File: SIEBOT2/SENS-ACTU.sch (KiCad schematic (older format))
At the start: 0 parts

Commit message: Added some fixes from AndroidStamp
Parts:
- added P? (x2): CONN_3X2, symbol CONN_3X2
- added P?: CONN_9X2, symbol CONN_9X2
- added P?: CONN_12X2, symbol CONN_12X2
- added P?: CONN_8X2, symbol CONN_8X2
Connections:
- new net GND: P?.2, P?.2, P?.5, P?.5
- new net I2C1_SCL_CONN: P?.4
- new net I2C1_SDA_CONN: P?.6
- new net I2C2_SCL_CONN: P?.3
- new net I2C2_SDA_CONN: P?.1
- new net STM32_ADC0: P?.1
- new net STM32_ADC1: P?.3
- new net STM32_ADC10: P?.12
- new net STM32_ADC11: P?.10
- new net STM32_ADC12: P?.8
- new net STM32_ADC13: P?.6
- new net STM32_ADC14: P?.4
- new net STM32_ADC15: P?.2
- new net STM32_ADC2: P?.5
- new net STM32_ADC3: P?.7
- new net STM32_ADC4: P?.9
- new net STM32_ADC5: P?.11
- new net STM32_ADC6: P?.13
- new net STM32_ADC7: P?.15
- new net STM32_ADC8: P?.16
- new net STM32_ADC9: P?.14
- new net STM32_PD10: P?.7
- new net STM32_PD11: P?.9
- new net STM32_PD3: P?.1
- new net STM32_PD4: P?.3
- new net STM32_PD7: P?.5
- new net STM32_PE1: P?.18
- new net STM32_PE10: P?.11
- new net STM32_PE12: P?.13
- new net STM32_PE14: P?.15
- new net STM32_PE15: P?.17
- new net STM32_PE2: P?.16
- new net STM32_PE3: P?.14
- new net STM32_PE4: P?.12
- new net STM32_PE5: P?.10
- new net STM32_PE6: P?.8
- new net STM32_PE7: P?.6
- new net STM32_PE8: P?.4
- new net STM32_PE9: P?.2
- new net TIM16_BKIN: P?.9 (P9)
- new net TIM16_CH1: P?.7 (P7)
- new net TIM17_CH1: P?.5 (P5)
- new net TIM1_BKIN: P?.2 (P2)
- new net TIM1_CH1: P?.14 (P14)
- new net TIM1_CH1N: P?.16 (P16)
- new net TIM1_CH2: P?.10 (P10)
- new net TIM1_CH2N: P?.12 (P12)
- new net TIM1_CH3: P?.6 (P6)
- new net TIM1_CH3N: P?.8 (P8)
- new net TIM1_CH4: P?.4 (P4)
- new net TIM1_ETR: P?.18 (P18)
- new net TIM2_CH1_ETR: P?.3 (P3)
- new net TIM2_CH2: P?.1 (P1)
- new net TIM3_CH1: P?.19 (P19)
- new net TIM3_CH2: P?.17 (P17)
- new net TIM3_CH3: P?.15 (P15)
- new net TIM3_CH4: P?.13 (P13)
- new net TIM3_ETR: P?.11 (P11)
- new net TIM4_CH1: P?.23 (P23)
- new net TIM4_CH2: P?.24 (P24)
- new net TIM4_CH3: P?.22 (P22)
- new net TIM4_CH4: P?.20 (P20)
- new net TIM4_ETR: P?.21 (P21)
- new net USART2_RX: P?.1, P?.6
- new net USART2_TX: P?.3, P?.4

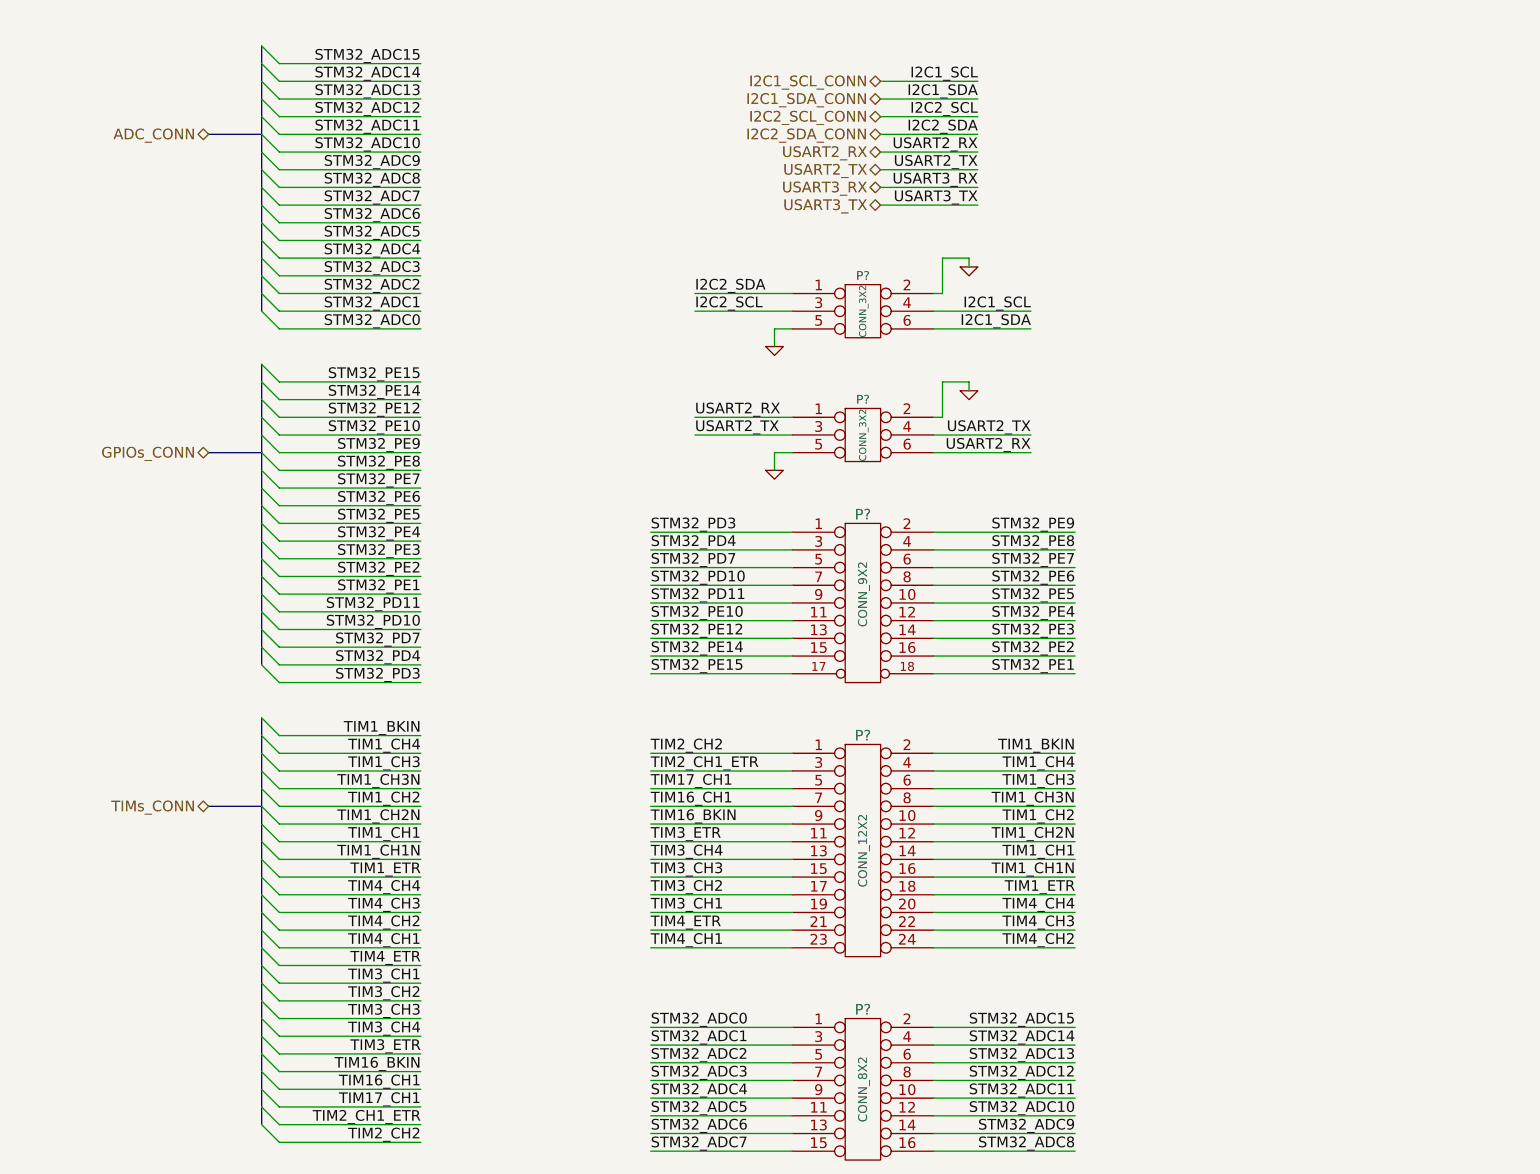
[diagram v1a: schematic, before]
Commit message: Added power dc-dc, fixed stm32 control pins
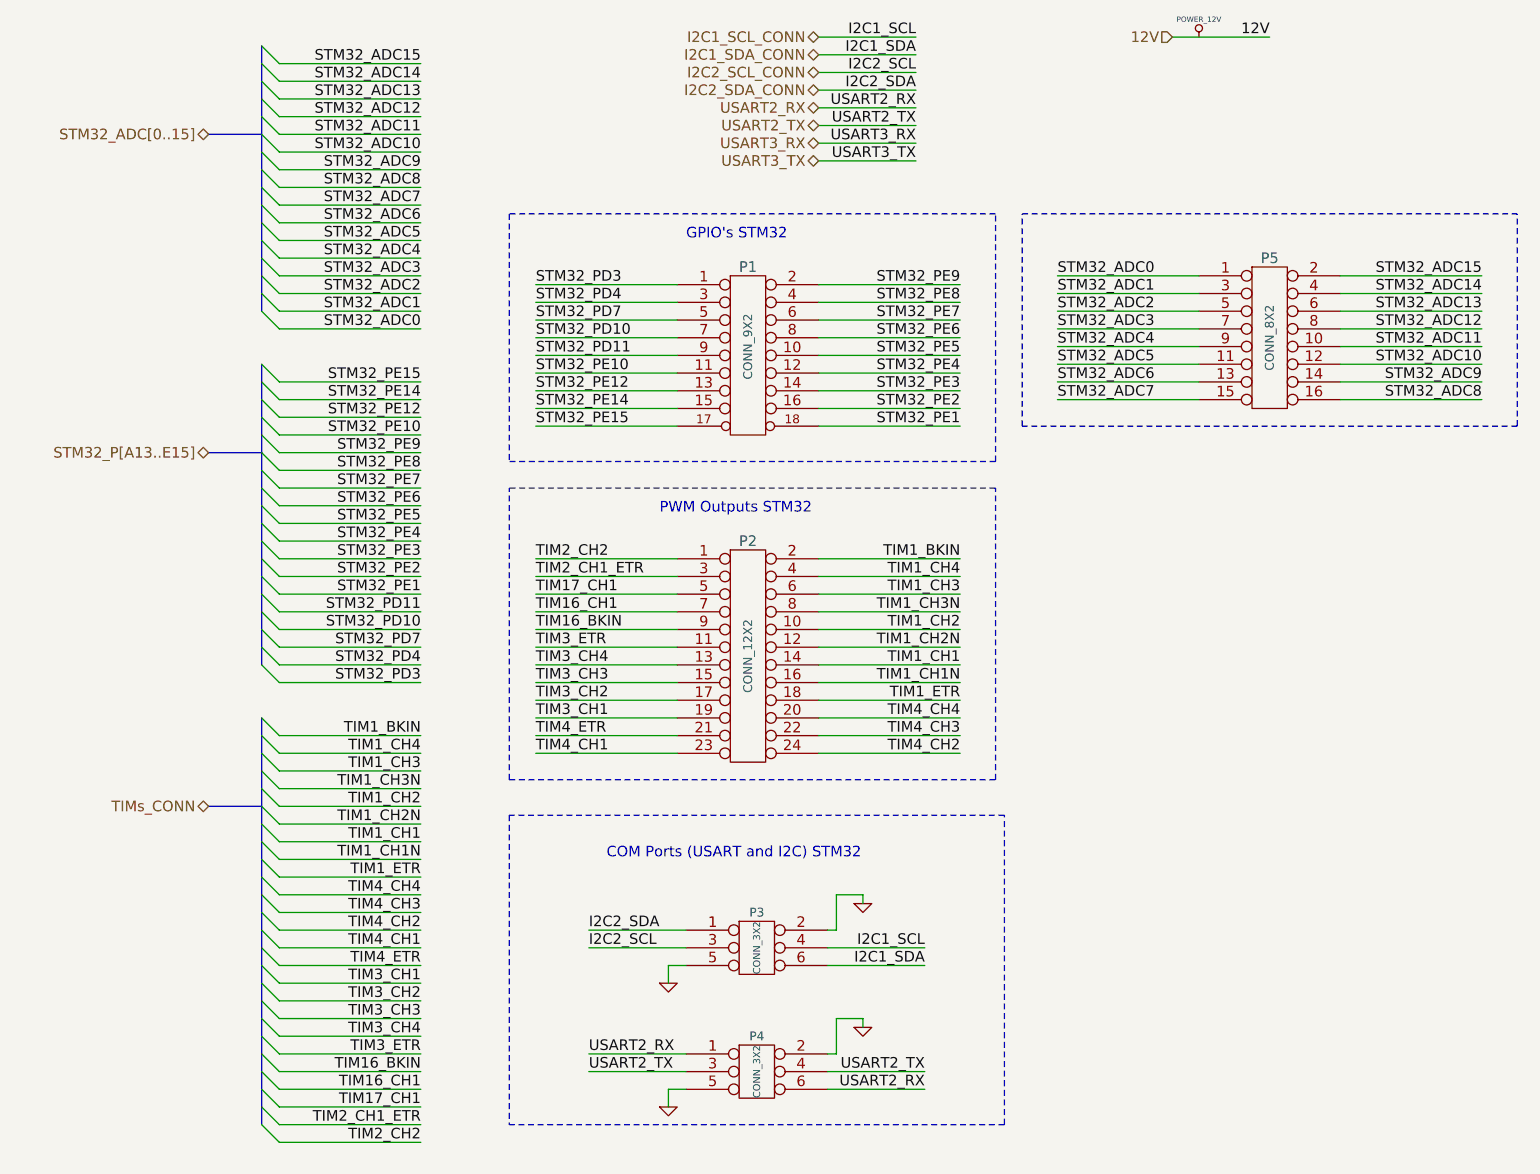
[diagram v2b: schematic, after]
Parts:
- gave numbers to parts that had none: 5
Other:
- note added: "COM Ports (USART and I2C) STM32"
- note added: "GPIO's STM32"
- note added: "PWM Outputs STM32"
- moved on the sheet: P1, P2, P3, P4, P5

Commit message: STM32 connection fixes + various fixes
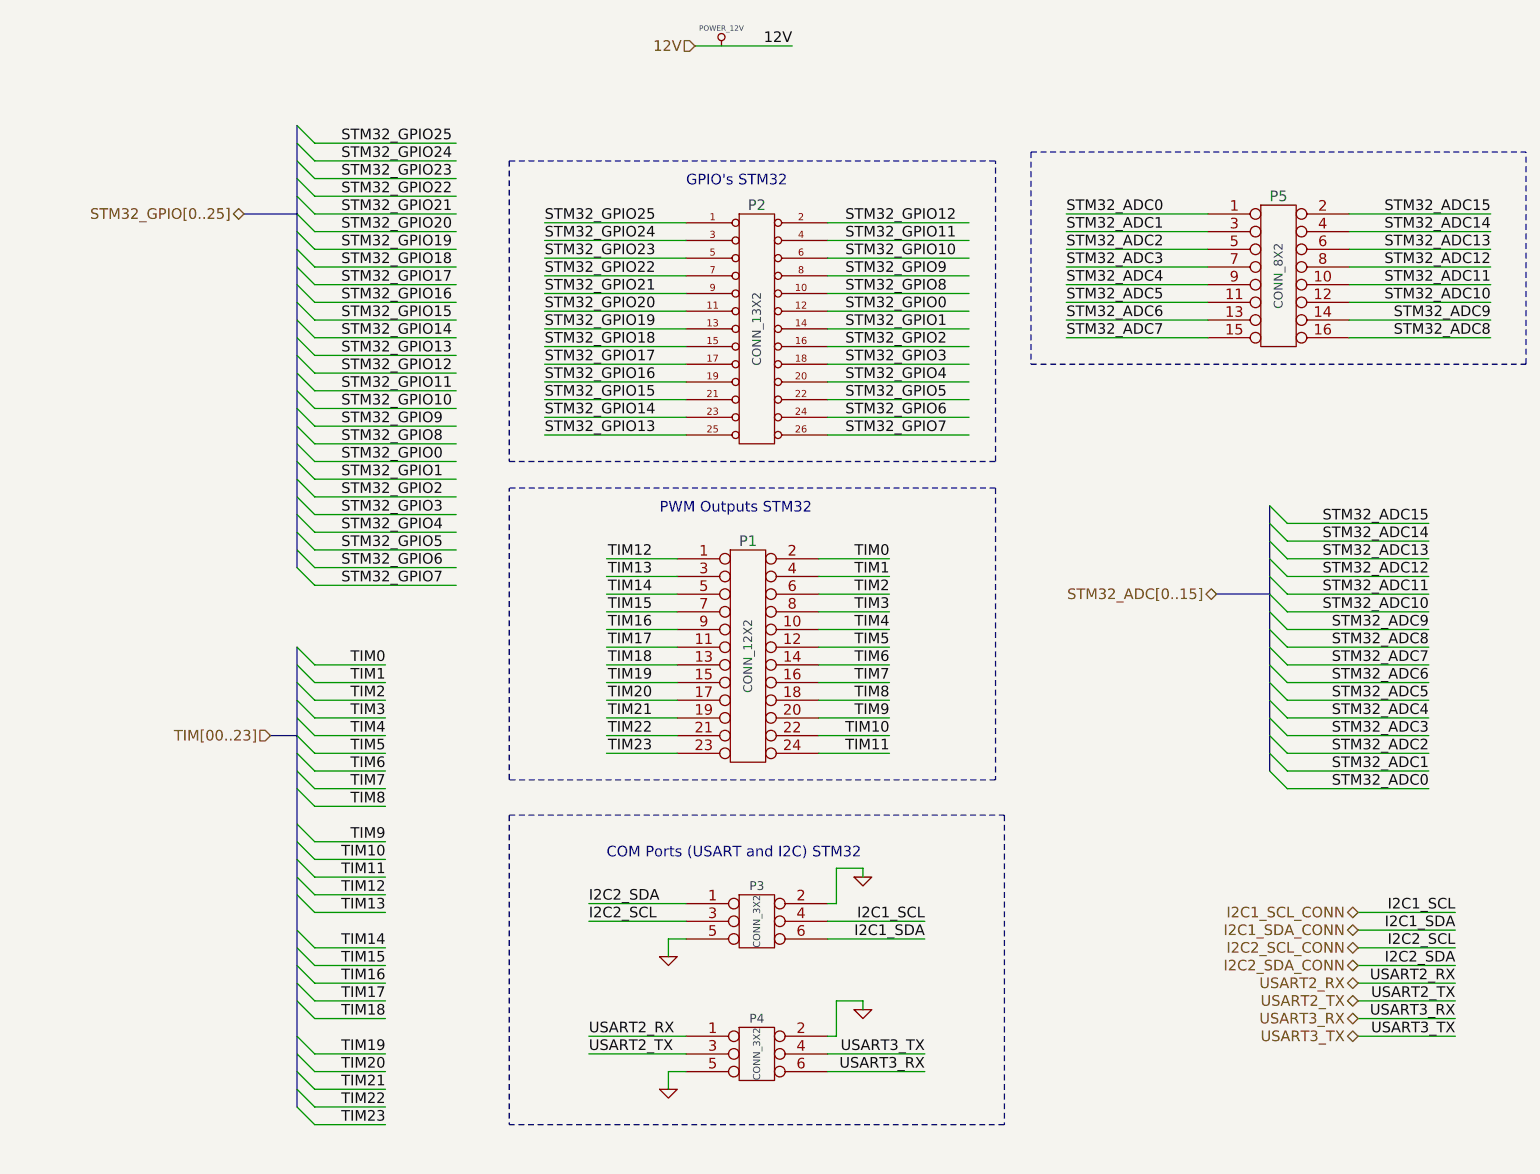
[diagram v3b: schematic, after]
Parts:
- removed P1: CONN_9X2, symbol CONN_9X2
- added P2: CONN_13X2, symbol CONN_13X2
- renumbered P2 to P1
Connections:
- net labels added: STM32_GPIO0, STM32_GPIO1, STM32_GPIO10, STM32_GPIO11, STM32_GPIO12, STM32_GPIO13, STM32_GPIO14, STM32_GPIO15, STM32_GPIO16, STM32_GPIO17, STM32_GPIO18, STM32_GPIO19, STM32_GPIO2, STM32_GPIO20, STM32_GPIO21, STM32_GPIO22, STM32_GPIO23, STM32_GPIO24, STM32_GPIO25, STM32_GPIO3, STM32_GPIO4, STM32_GPIO5, STM32_GPIO6, STM32_GPIO7, STM32_GPIO8, STM32_GPIO9, STM32_GPIO[0..25], TIM0, TIM1, TIM10, TIM11, TIM12, TIM13, TIM14, TIM15, TIM16, TIM17, TIM18, TIM19, TIM2, TIM20, TIM21, TIM22, TIM23, TIM3, TIM4, TIM5, TIM6, TIM7, TIM8, TIM9, TIM[00..23]
- net labels removed: STM32_PD10, STM32_PD11, STM32_PD3, STM32_PD4, STM32_PD7, STM32_PE1, STM32_PE10, STM32_PE12, STM32_PE14, STM32_PE15, STM32_PE2, STM32_PE3, STM32_PE4, STM32_PE5, STM32_PE6, STM32_PE7, STM32_PE8, STM32_PE9, STM32_P[A13..E15], TIM16_BKIN, TIM16_CH1, TIM17_CH1, TIM1_BKIN, TIM1_CH1, TIM1_CH1N, TIM1_CH2, TIM1_CH2N, TIM1_CH3, TIM1_CH3N, TIM1_CH4, TIM1_ETR, TIM2_CH1_ETR, TIM2_CH2, TIM3_CH1, TIM3_CH2, TIM3_CH3, TIM3_CH4, TIM3_ETR, TIM4_CH1, TIM4_CH2, TIM4_CH3, TIM4_CH4, TIM4_ETR, TIMs_CONN
- wire segments 145 -> 161
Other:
- moved on the sheet: P3, P4, P5
